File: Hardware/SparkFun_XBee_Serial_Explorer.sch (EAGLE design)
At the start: 42 parts, among them J1 POWER_JACKPTH, Q1 MBT2222, U1 MAX232SOIC16, U2 XBEE-1B3, U3 LM317, X1 RS232

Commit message: Board rev in progress
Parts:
- LOGO2: value SFE_LOGO_NAME_FLAME.1_INCH -> SFE_LOGO_NAME_FLAME.2_INCH; device SparkFun-Aesthetics:SFE_LOGO_NAME_FLAME.1_INCH -> SparkFun-Aesthetics:SFE_LOGO_NAME_FLAME.2_INCH
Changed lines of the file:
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@@
 <grid distance="0.1" unitdist="inch" unit="inch" style="lines" multiple="1" display="no" altdistance="0.01" altunitdist="inch" altunit="inch"/>
 <layers>
-<layer number="1" name="Top" color="4" fill="1" visible="yes" active="no"/>
-<layer number="2" name="Route2" color="1" fill="3" visible="yes" active="no"/>
-<layer number="3" name="Route3" color="4" fill="3" visible="yes" active="no"/>
-<layer number="4" name="Route4" color="1" fill="4" visible="yes" active="no"/>
-<layer number="5" name="Route5" color="4" fill="4" visible="yes" active="no"/>
-<layer number="6" name="Route6" color="1" fill="8" visible="yes" active="no"/>
-<layer number="7" name="Route7" color="4" fill="8" visible="yes" active="no"/>
-<layer number="8" name="Route8" color="1" fill="2" visible="yes" active="no"/>
-<layer number="9" name="Route9" color="4" fill="2" visible="yes" active="no"/>
-<layer number="10" name="Route10" color="1" fill="7" visible="yes" active="no"/>
-<layer number="11" name="Route11" color="4" fill="7" visible="yes" active="no"/>
-<layer number="12" name="Route12" color="1" fill="5" visible="yes" active="no"/>
-<layer number="13" name="Route13" color="4" fill="5" visible="yes" active="no"/>
-<layer number="14" name="Route14" color="1" fill="6" visible="yes" active="no"/>
-<layer number="15" name="Route15" color="4" fill="6" visible="yes" active="no"/>
-<layer number="16" name="Bottom" color="1" fill="1" visible="yes" active="no"/>
-<layer number="17" name="Pads" color="2" fill="1" visible="yes" active="no"/>
-<layer number="18" name="Vias" color="2" fill="1" visible="yes" active="no"/>
-<layer number="19" name="Unrouted" color="6" fill="1" visible="yes" active="no"/>
-<layer number="20" name="Dimension" color="15" fill="1" visible="yes" active="no"/>
-<layer number="21" name="tPlace" color="16" fill="1" visible="yes" active="no"/>
-<layer number="22" name="bPlace" color="14" fill="1" visible="yes" active="no"/>
-<layer number="23" name="tOrigins" color="15" fill="1" visible="yes" active="no"/>
-<layer number="24" name="bOrigins" color="15" fill="1" visible="yes" active="no"/>
-<layer number="25" name="tNames" color="7" fill="1" visible="yes" active="no"/>
-<layer number="26" name="bNames" color="7" fill="1" visible="yes" active="no"/>
-<layer number="27" name="tValues" color="7" fill="1" visible="yes" active="no"/>
-<layer number="28" name="bValues" color="7" fill="1" visible="yes" active="no"/>
+<layer number="1" name="Top" color="4" fill="1" visible="no" active="no"/>
+<layer number="2" name="Route2" color="1" fill="3" visible="no" active="no"/>
+<layer number="3" name="Route3" color="4" fill="3" visible="no" active="no"/>
+<layer number="4" name="Route4" color="1" fill="4" visible="no" active="no"/>
+<layer number="5" name="Route5" color="4" fill="4" visible="no" active="no"/>
+<layer number="6" name="Route6" color="1" fill="8" visible="no" active="no"/>
+<layer number="7" name="Route7" color="4" fill="8" visible="no" active="no"/>
+<layer number="8" name="Route8" color="1" fill="2" visible="no" active="no"/>
+<layer number="9" name="Route9" color="4" fill="2" visible="no" active="no"/>
+<layer number="10" name="Route10" color="1" fill="7" visible="no" active="no"/>
+<layer number="11" name="Route11" color="4" fill="7" visible="no" active="no"/>
+<layer number="12" name="Route12" color="1" fill="5" visible="no" active="no"/>
+<layer number="13" name="Route13" color="4" fill="5" visible="no" active="no"/>
+<layer number="14" name="Route14" color="1" fill="6" visible="no" active="no"/>
+<layer number="15" name="Route15" color="4" fill="6" visible="no" active="no"/>
+<layer number="16" name="Bottom" color="1" fill="1" visible="no" active="no"/>
+<layer number="17" name="Pads" color="2" fill="1" visible="no" active="no"/>
+<layer number="18" name="Vias" color="2" fill="1" visible="no" active="no"/>
+<layer number="19" name="Unrouted" color="6" fill="1" visible="no" active="no"/>
+<layer number="20" name="Dimension" color="15" fill="1" visible="no" active="no"/>
+<layer number="21" name="tPlace" color="16" fill="1" visible="no" active="no"/>
+<layer number="22" name="bPlace" color="14" fill="1" visible="no" active="no"/>
+<layer number="23" name="tOrigins" color="15" fill="1" visible="no" active="no"/>
+<layer number="24" name="bOrigins" color="15" fill="1" visible="no" active="no"/>
+<layer number="25" name="tNames" color="7" fill="1" visible="no" active="no"/>
+<layer number="26" name="bNames" color="7" fill="1" visible="no" active="no"/>
+<layer number="27" name="tValues" color="7" fill="1" visible="no" active="no"/>
+<layer number="28" name="bValues" color="7" fill="1" visible="no" active="no"/>
 <layer number="29" name="tStop" color="7" fill="3" visible="no" active="no"/>
 <layer number="30" name="bStop" color="7" fill="6" visible="no" active="no"/>
@@
 <layer number="35" name="tGlue" color="7" fill="4" visible="no" active="no"/>
 <layer number="36" name="bGlue" color="7" fill="5" visible="no" active="no"/>
-<layer number="37" name="tTest" color="7" fill="1" visible="yes" active="no"/>
-<layer number="38" name="bTest" color="7" fill="1" visible="yes" active="no"/>
+<layer number="37" name="tTest" color="7" fill="1" visible="no" active="no"/>
+<layer number="38" name="bTest" color="7" fill="1" visible="no" active="no"/>
 <layer number="39" name="tKeepout" color="4" fill="11" visible="no" active="no"/>
 <layer number="40" name="bKeepout" color="1" fill="11" visible="no" active="no"/>
@@
 <layer number="44" name="Drills" color="7" fill="1" visible="no" active="no"/>
 <layer number="45" name="Holes" color="7" fill="1" visible="no" active="no"/>
-<layer number="46" name="Milling" color="3" fill="1" visible="yes" active="no"/>
-<layer number="47" name="Measures" color="7" fill="1" visible="yes" active="no"/>
-<layer number="48" name="Document" color="7" fill="1" visible="yes" active="no"/>
-<layer number="49" name="Reference" color="7" fill="1" visible="yes" active="no"/>
-<layer number="50" name="dxf" color="7" fill="1" visible="yes" active="no"/>
-<layer number="51" name="tDocu" color="6" fill="1" visible="yes" active="no"/>
-<layer number="52" name="bDocu" color="7" fill="1" visible="yes" active="no"/>
-<layer number="53" name="tGND_GNDA" color="7" fill="9" visible="yes" active="no"/>
-<layer number="54" name="bGND_GNDA" color="1" fill="9" visible="yes" active="no"/>
-<layer number="56" name="wert" color="7" fill="1" visible="yes" active="no"/>
-<layer number="57" name="tCAD" color="7" fill="1" visible="yes" active="no"/>
+<layer number="46" name="Milling" color="3" fill="1" visible="no" active="no"/>
+<layer number="47" name="Measures" color="7" fill="1" visible="no" active="no"/>
+<layer number="48" name="Document" color="7" fill="1" visible="no" active="no"/>
+<layer number="49" name="Reference" color="7" fill="1" visible="no" active="no"/>
+<layer number="50" name="dxf" color="7" fill="1" visible="no" active="no"/>
+<layer number="51" name="tDocu" color="6" fill="1" visible="no" active="no"/>
+<layer number="52" name="bDocu" color="7" fill="1" visible="no" active="no"/>
+<layer number="53" name="tGND_GNDA" color="7" fill="9" visible="no" active="no"/>
+<layer number="54" name="bGND_GNDA" color="1" fill="9" visible="no" active="no"/>
+<layer number="56" name="wert" color="7" fill="1" visible="no" active="no"/>
+<layer number="57" name="tCAD" color="7" fill="1" visible="no" active="no"/>
 <layer number="91" name="Nets" color="2" fill="1" visible="yes" active="yes"/>
 <layer number="92" name="Busses" color="1" fill="1" visible="yes" active="yes"/>
@@
 <part name="U$1" library="SparkFun-Aesthetics" deviceset="REVISION" device=""/>
 <part name="LOGO1" library="SparkFun-Aesthetics" deviceset="OSHW-LOGO" device="L"/>
-<part name="LOGO2" library="SparkFun-Aesthetics" deviceset="SFE_LOGO_NAME_FLAME" device=".1_INCH" value="SFE_LOGO_NAME_FLAME.1_INCH"/>
+<part name="LOGO2" library="SparkFun-Aesthetics" deviceset="SFE_LOGO_NAME_FLAME" device=".2_INCH" value="SFE_LOGO_NAME_FLAME.2_INCH"/>
 <part name="GND15" library="SparkFun-Aesthetics" deviceset="GND" device=""/>
 </parts>

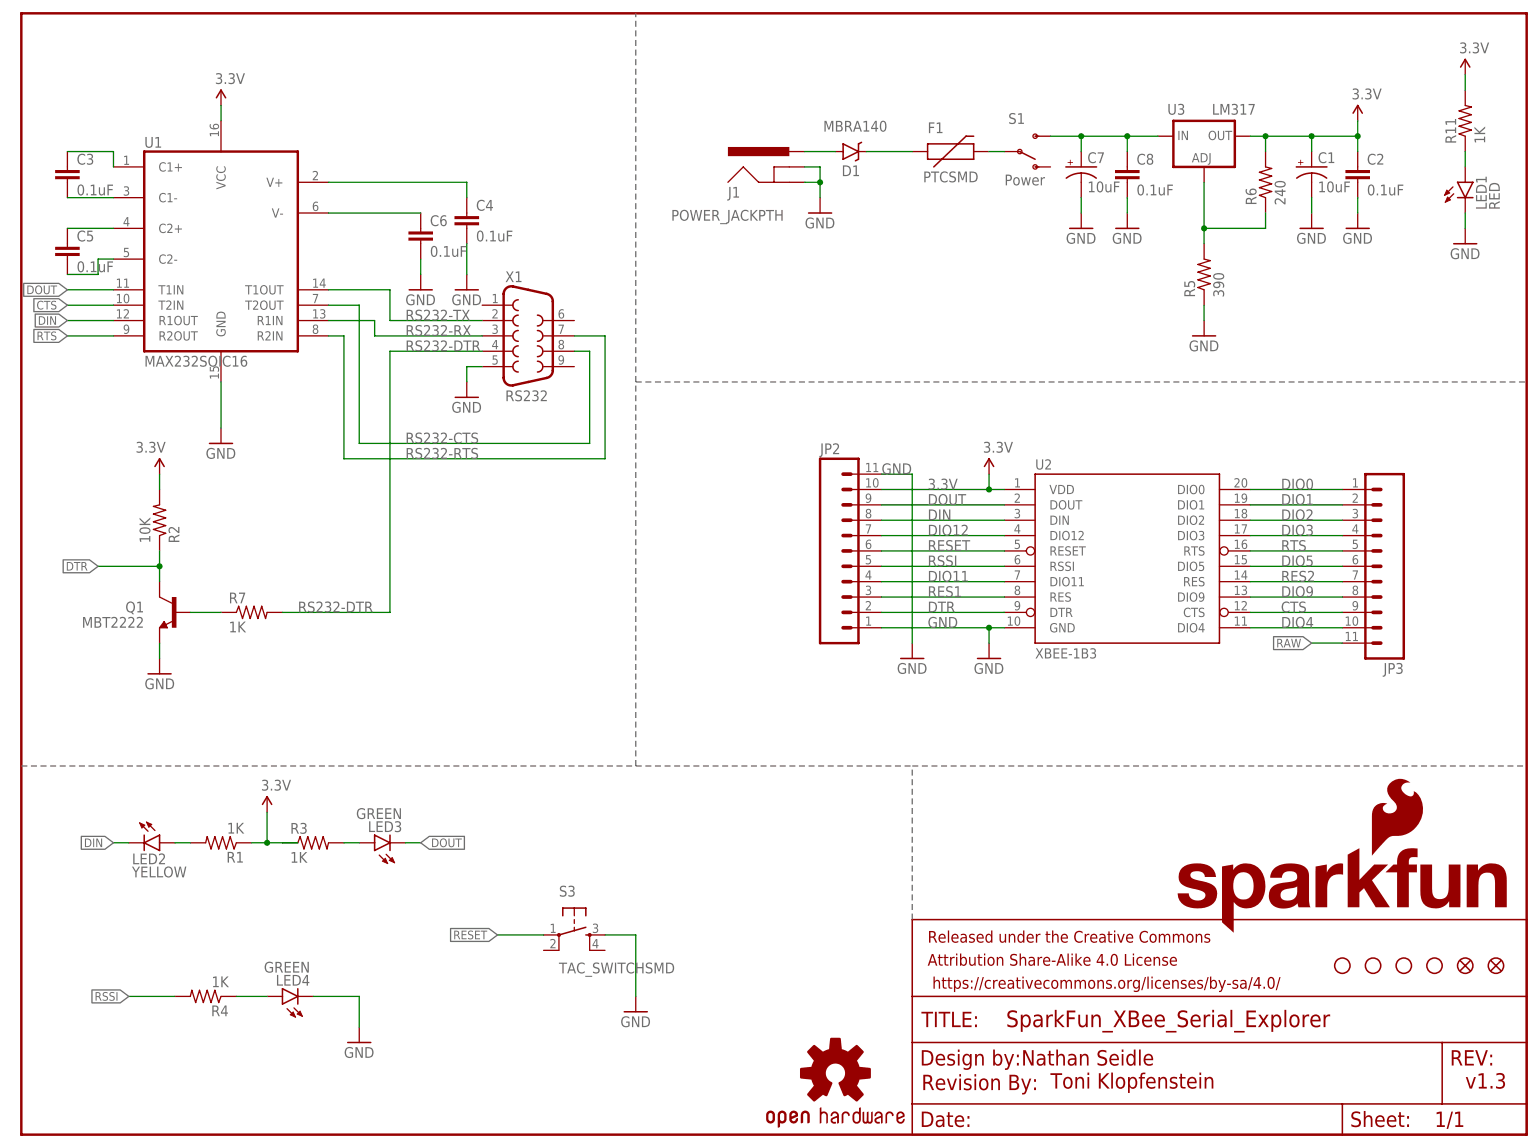
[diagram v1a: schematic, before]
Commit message: Rerouting, updating parts to PTH, add dimensions, etc.
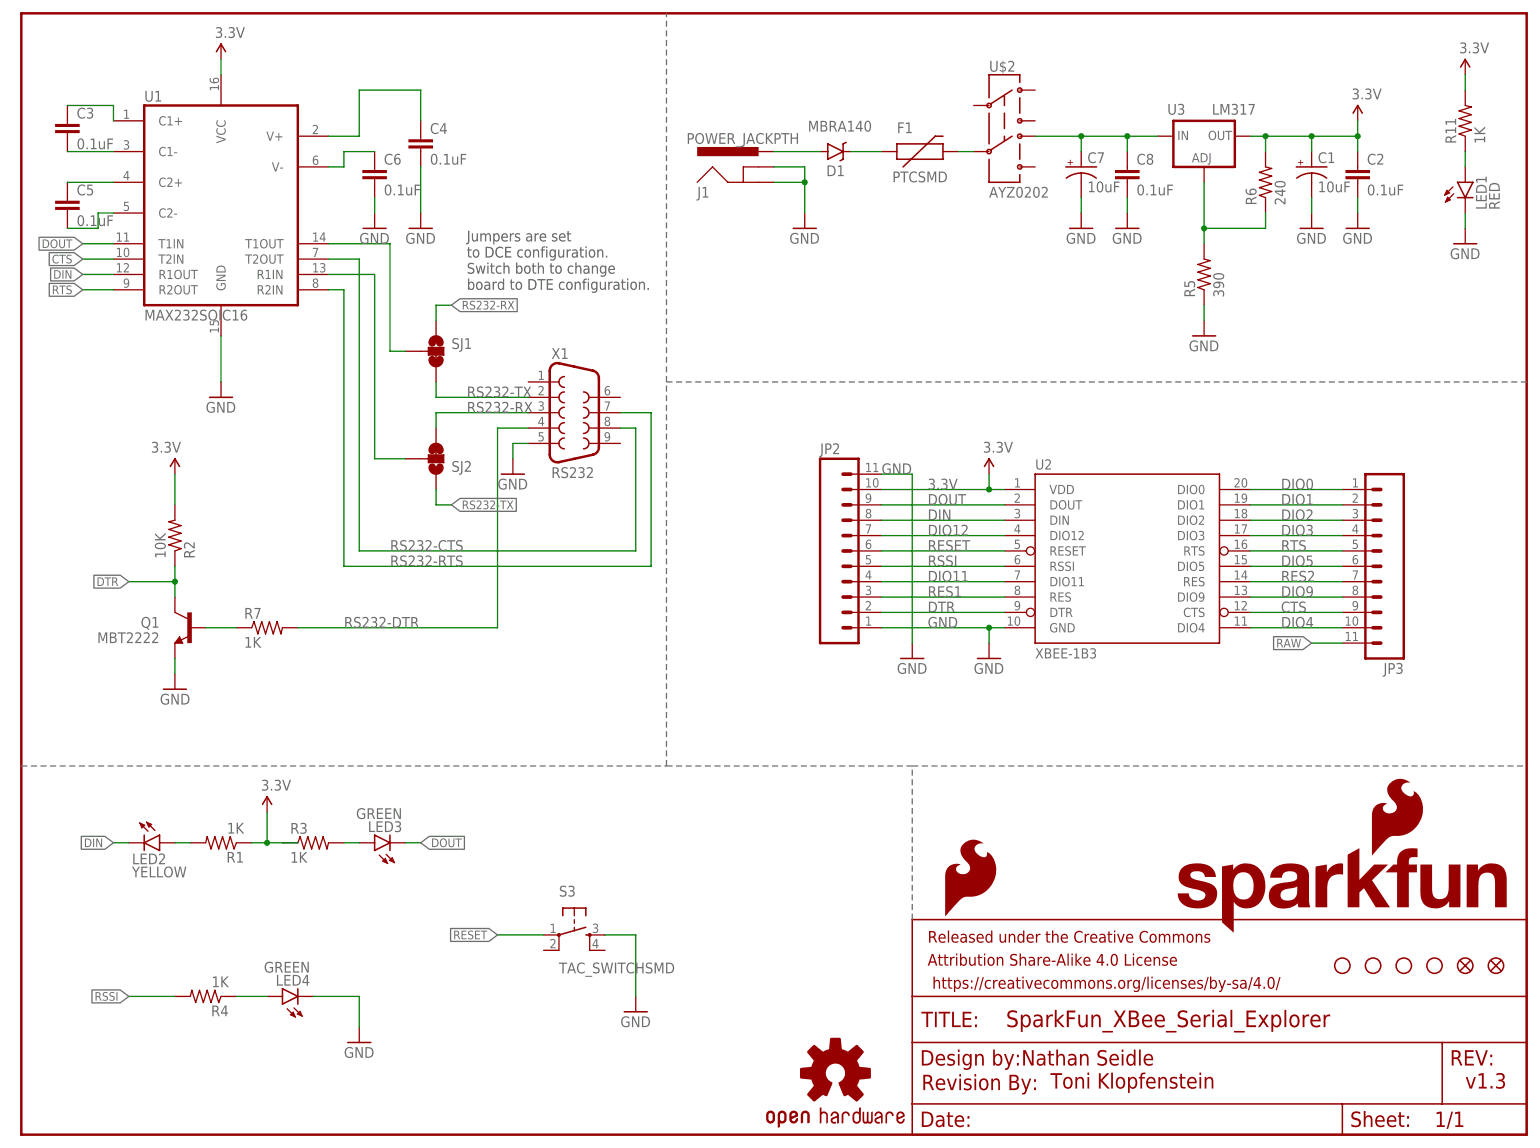
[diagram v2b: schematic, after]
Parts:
- removed S1: Power, SparkFun:SWITCH-SPSTSMD
- added LOGO3: SFE_LOGO_FLAME.1_INCH, SparkFun-Aesthetics:SFE_LOGO_FLAME.1_INCH
- added SJ1, SJ2: JUMPER-PAD-3-2OF3_NC_BY_TRACE_SMALL, SparkFun-Passives:JUMPER-PAD-3-2OF3_NC_BY_TRACE_SMALL
- added U$2: AYZ0202, SparkFun-Electromechanical:AYZ0202
- F1: device SparkFun:PTCSMD -> SparkFun-PowerIC:PTCSMD
- U$10, U$11, U$5, U$9: device SparkFun:STAND-OFF -> SparkFun-Electromechanical:STAND-OFF
- U$16, U$7: device SparkFun:FIDUCIAL1X2 -> SparkFun-Aesthetics:FIDUCIAL1X2
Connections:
- new net N$13: SJ2.2, U1.R1IN
- new net N$14: SJ1.2, U1.T1OUT
- net N$11: now also U$2.5; no longer S1.P
- net RAW: now also U$2.4; no longer S1.S
- net RS232-RX: now also SJ1.1, SJ2.3; no longer U1.R1IN
- net RS232-TX: now also SJ1.3, SJ2.1; no longer U1.T1OUT
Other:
- note added: "Jumpers are set to DCE configuration. Switch both to change board to DTE configuration."
- moved on the sheet: C3, C4, C5, C6, D1, F1, J1, Q1, R2, R7, U1, X1

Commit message: Updating board and schematic to address GitHub issues
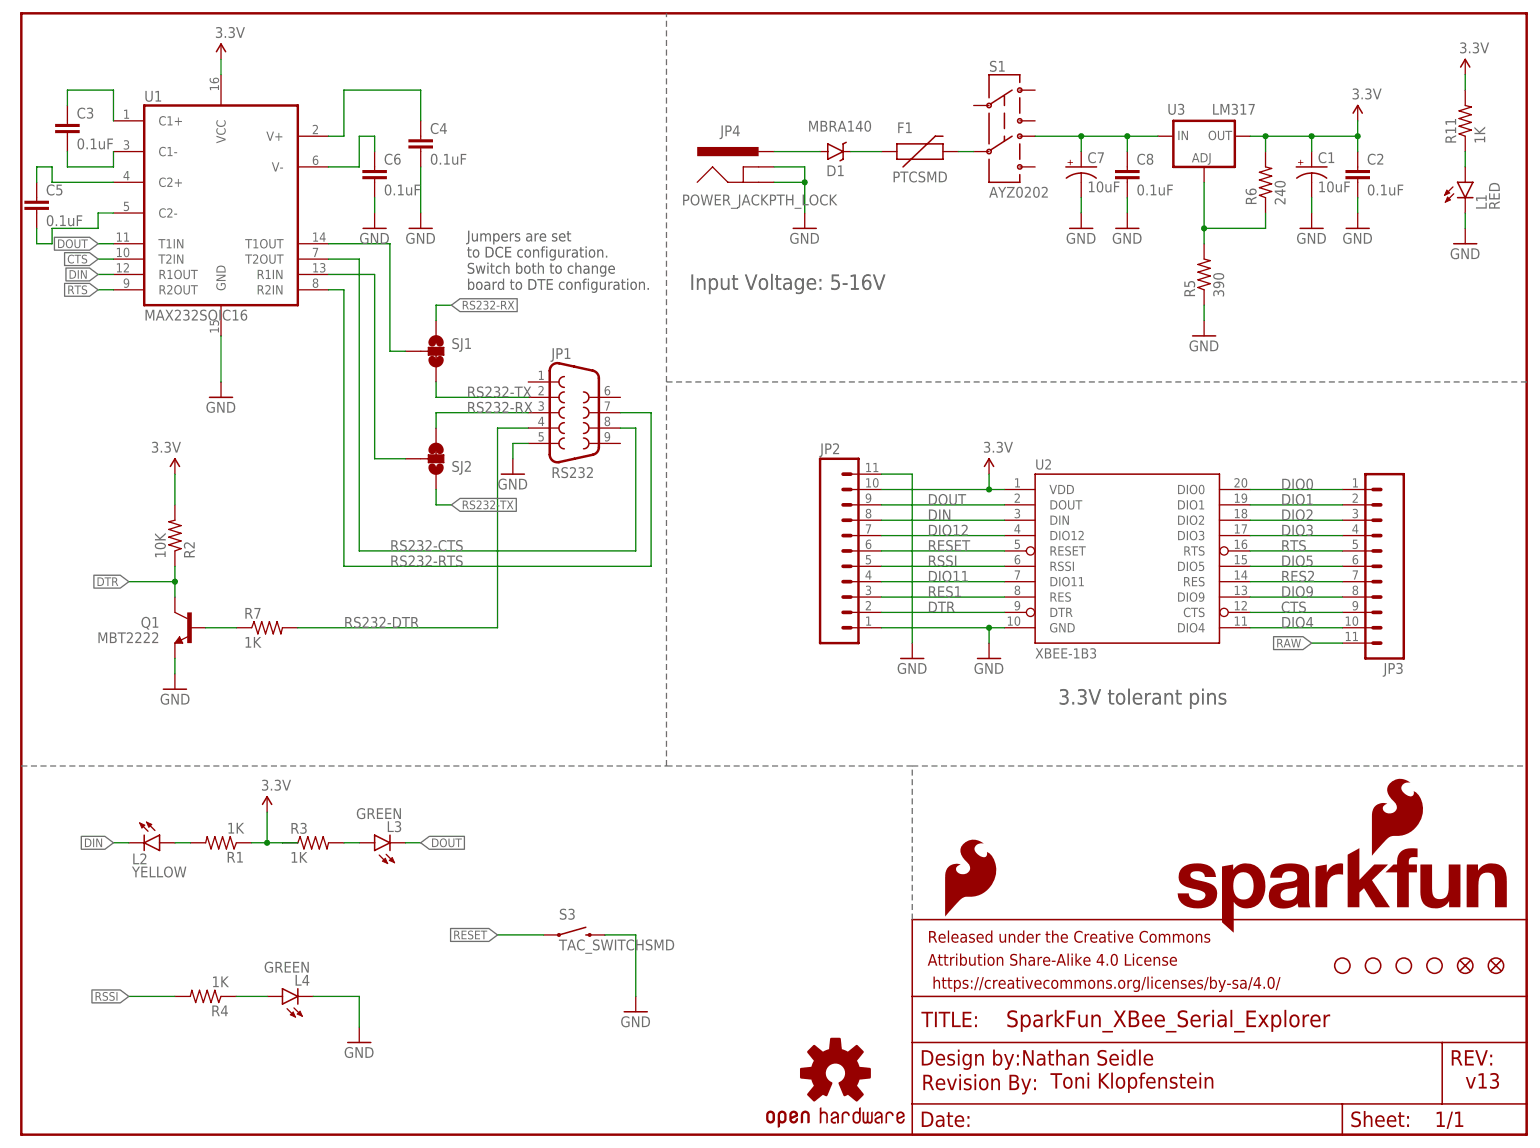
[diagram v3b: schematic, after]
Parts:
- removed J1: POWER_JACKPTH, SparkFun-Connectors:POWER_JACKPTH
- added JP4: POWER_JACKPTH_LOCK, SparkFun-Connectors:POWER_JACKPTH_LOCK
- R1, R11, R3, R4, R7: device SparkFun-Resistors:1KOHM1/10W1%(0603) -> SparkFun-Resistors:1KOHM-1/10W-1%(0603)
- R2: device SparkFun-Resistors:10KOHM1/10W1%(0603)0603 -> SparkFun-Resistors:10KOHM-1/10W-1%(0603)0603
- S3: device SparkFun-Electromechanical:TAC_SWITCHSMD -> SparkFun-Electromechanical:SWITCH-MOMENTARY-2SMD-REDUNDANT
- renumbered LED1 to L1, LED2 to L2, LED3 to L3, LED4 to L4, U$2 to S1, X1 to JP1
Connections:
- net GND: now also JP4.GND, JP4.GNDBREAK, S3.2; no longer J1.GND, J1.GNDBREAK, S3.3
- net N$15: now also JP4.PWR; no longer J1.PWR
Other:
- note added: "3.3V tolerant pins"
- note added: "Input Voltage: 5-16V"
- note added: "v13"
- note removed: "v1.3"
- moved on the sheet: C5
